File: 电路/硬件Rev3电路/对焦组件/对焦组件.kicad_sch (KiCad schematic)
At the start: 1 part, among them U1 CH32V003FxPx

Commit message: 对焦驱动几乎完成
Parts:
- removed U1: CH32V003FxPx, Package_SO:TSSOP-20_4.4x6.5mm_P0.65mm, symbol MCU_WCH_RiscV:CH32V003FxPx
- added C1, C11, C6, C7: 100nf, Capacitor_SMD:C_0603_1608Metric, symbol Device:C
- added C10, C9: 10uf, Capacitor_SMD:C_0805_2012Metric, symbol Device:C
- added C12, C13, C14, C15, C16, C17, C18: 22uf, Capacitor_SMD:C_0603_1608Metric, symbol Device:C
- added C2: 22uf, Capacitor_Tantalum_SMD:CP_EIA-3216-18_Kemet-A, symbol Device:C_Polarized
- added C3: 1uf, Capacitor_SMD:C_0603_1608Metric, symbol Device:C
- added C4, C5: 20pf, Capacitor_SMD:C_0603_1608Metric, symbol Device:C
- added C8: 47uf, Capacitor_SMD:C_0805_2012Metric, symbol Device:C
- added CN1: HX SH-1.0-8PWT, EasyEDA:CONN-SMD_8P-P1.00_HX-SH1.0-8PWT, symbol EasyEDA:HXSH-1.0-8PWT
- added CN2: HX SH-1.0-4PWT, EasyEDA:CONN-SMD_4P-HX-SH-1.0-4PWT, symbol EasyEDA:HXSH-1.0-4PWT
- added FB1: FerriteBead, Inductor_SMD:L_0603_1608Metric, symbol Device:FerriteBead
- added H1, H2, H3, H4: MountingHole, MountingHole:MountingHole_2.2mm_M2, symbol Mechanical:MountingHole
- added J1: Conn_01x04_Pin, Connector_PinHeader_1.27mm:PinHeader_1x04_P1.27mm_Vertical, symbol Connector:Conn_01x04_Pin
- added L1: 2.2uH, Inductor_SMD:L_Coilcraft_1008HQ_2520Metric, symbol Device:L
- added R1, R2, R3, R4: 10k, Resistor_SMD:R_0603_1608Metric, symbol Device:R
- added R10, R11, R6, R7, R9: 10k 1%, Resistor_SMD:R_0603_1608Metric, symbol Device:R
- added R12: 1k, Resistor_SMD:R_0603_1608Metric, symbol Device:R
- added R5: 33.2k, Resistor_SMD:R_0603_1608Metric, symbol Device:R
- added R8: 2.2k 1%, Resistor_SMD:R_0603_1608Metric, symbol Device:R
- added TH1: Thermistor_NTC, Resistor_SMD:R_0603_1608Metric, symbol Device:Thermistor_NTC
- added TP2: BOOT, TestPoint:TestPoint_Pad_D1.0mm, symbol Connector:TestPoint
- added TP3: GND, TestPoint:TestPoint_Pad_D1.0mm, symbol Connector:TestPoint
- added TP4: 3.3V, TestPoint:TestPoint_Pad_D1.0mm, symbol Connector:TestPoint
- added TP5: NRST, TestPoint:TestPoint_Pad_D1.0mm, symbol Connector:TestPoint
- added TP6: VREF, TestPoint:TestPoint_Pad_D1.0mm, symbol Connector:TestPoint
- added U1: DRV8251ADDAR, EasyEDA:SOPOWERPAD-8_L4.9-W3.9-P1.27-LS6.0-TL-EP, symbol EasyEDA:DRV8251ADDAR
- added U2: STM32F030F4Px, Package_SO:TSSOP-20_4.4x6.5mm_P0.65mm, symbol MCU_ST_STM32F0:STM32F030F4Px
- added U3: TPS563201, Package_TO_SOT_SMD:SOT-23-6, symbol Regulator_Switching:TPS563201
- added Y1: 8Mhz, Crystal:Crystal_SMD_5032-2Pin_5.0x3.2mm, symbol Device:Crystal
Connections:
- new net: R4.1, R5.2, U3.4 (VFB)
- new net: TP5.1, U2.4 (NRST)
- new net: R12.2, R2.1, U1.1 (IPROPI)
- new net: C6.1, FB1.2, TP6.1, U2.5 (VDDA)
- new net: R1.2, TP2.1, U2.1 (BOOT0)
- new net: R3.1, U3.5 (EN)
- new net: C4.1, U2.2 (PF0), Y1.2
- new net: C5.1, U2.3 (PF1), Y1.1
- new net: C11.1, L1.1, U3.2 (SW)
- new net: C11.2, U3.6 (VBST)
- new net +3V3: C1.1, C12.1, C13.1, C14.1, C2.1, C3.1, FB1.1, J1.1 (Pin_1), L1.2, R10.2, R11.2, R5.1, R8.2, TP4.1, U1.4 (VREF), U2.16 (VDD)
- new net +6V: C10.1, C7.1, C8.1, C9.1, CN1.6, CN1.7, CN1.8, R3.2, R6.2, U1.5 (VM), U3.3 (VIN)
- new net ADC_3V3: C16.1, R8.1, R9.2, U2.7 (PA1)
- new net ADC_6V: C15.1, R6.1, R7.2, U2.11 (PA5)
- new net ADC_MT: R12.1, U2.12 (PA6)
- new net ADC_NTC1: C18.1, CN2.3, R10.1, U2.6 (PA0)
- new net ADC_NTC2: C17.1, R11.1, TH1.1, U2.10 (PA4)
- new net GND: C1.2, C10.2, C12.2, C13.2, C14.2, C15.2, C16.2, C17.2, C18.2, C2.2, C3.2, C4.2, C5.2, C6.2, C7.2, C8.2, C9.2, CN1.1, CN1.2, CN1.3, CN2.4, J1.4 (Pin_4), R1.1, R2.2, R4.2, R7.1, R9.1, TH1.2, TP3.1, U1.7 (GND), U1.9 (PAD), U2.15 (VSS), U3.1 (GND)
- new net MOT_A: CN2.1, U1.6 (OUT1)
- new net MOT_B: CN2.2, U1.8 (OUT2)
- new net MotorPWM_A: U1.3 (IN1), U2.18 (PA10)
- new net MotorPWM_B: U1.2 (IN2), U2.17 (PA9)
- new net SWCLK: J1.3 (Pin_3), U2.20 (PA14)
- new net SWDIO: J1.2 (Pin_2), U2.19 (PA13)
- new net USART1 _RX: CN1.4, U2.9 (PA3)
- new net USART1 _TX: CN1.5, U2.8 (PA2)
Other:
- note added: "ADC_IN0"
- note added: "ADC_IN1"
- note added: "ADC_IN4"
- note added: "ADC_IN5"
- note added: "ADC_IN6"
- note added: "TIM1_CH2"
- note added: "TIM1_CH3"

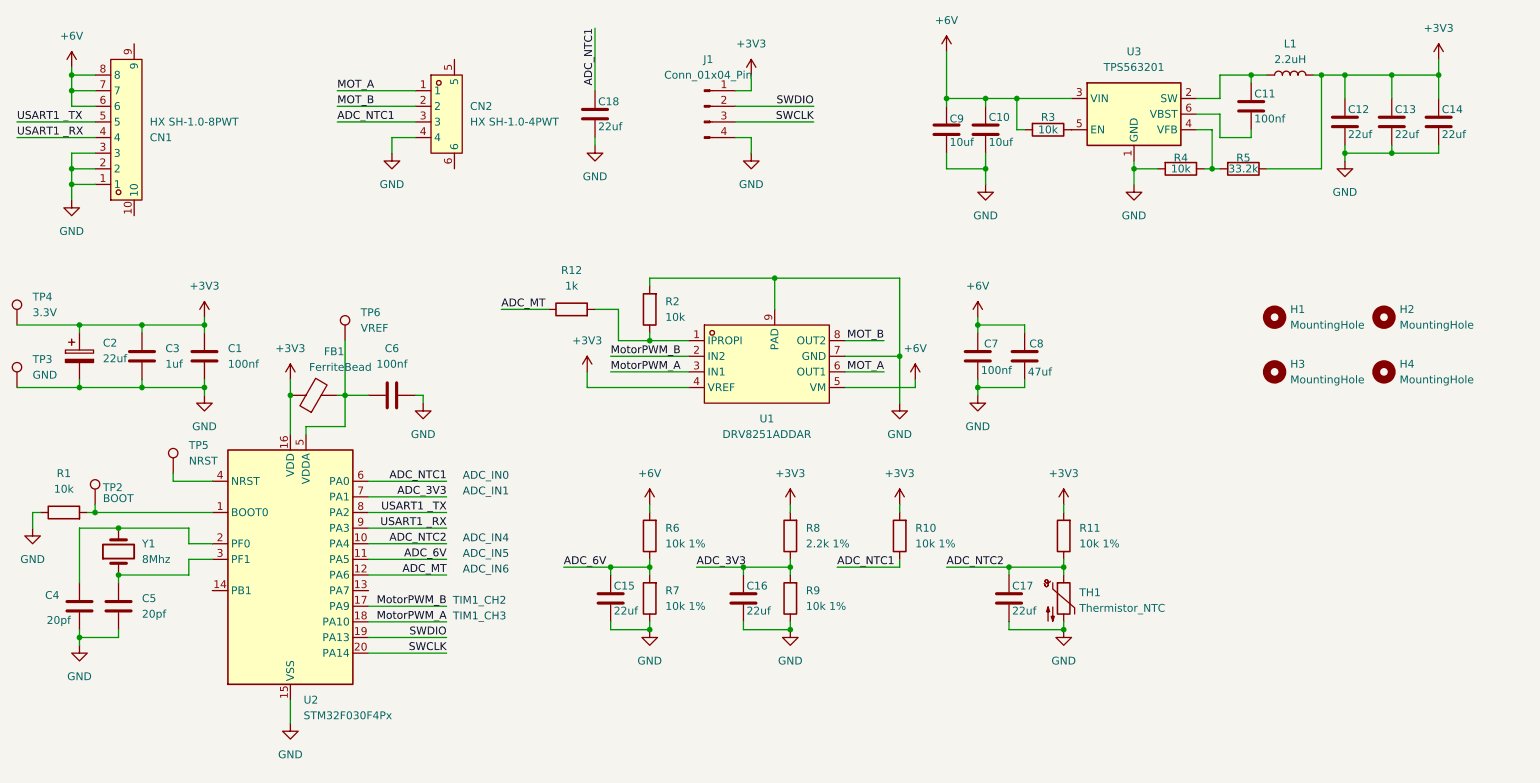
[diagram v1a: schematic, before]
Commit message: 对焦组件R1投产，对焦机构开始测试
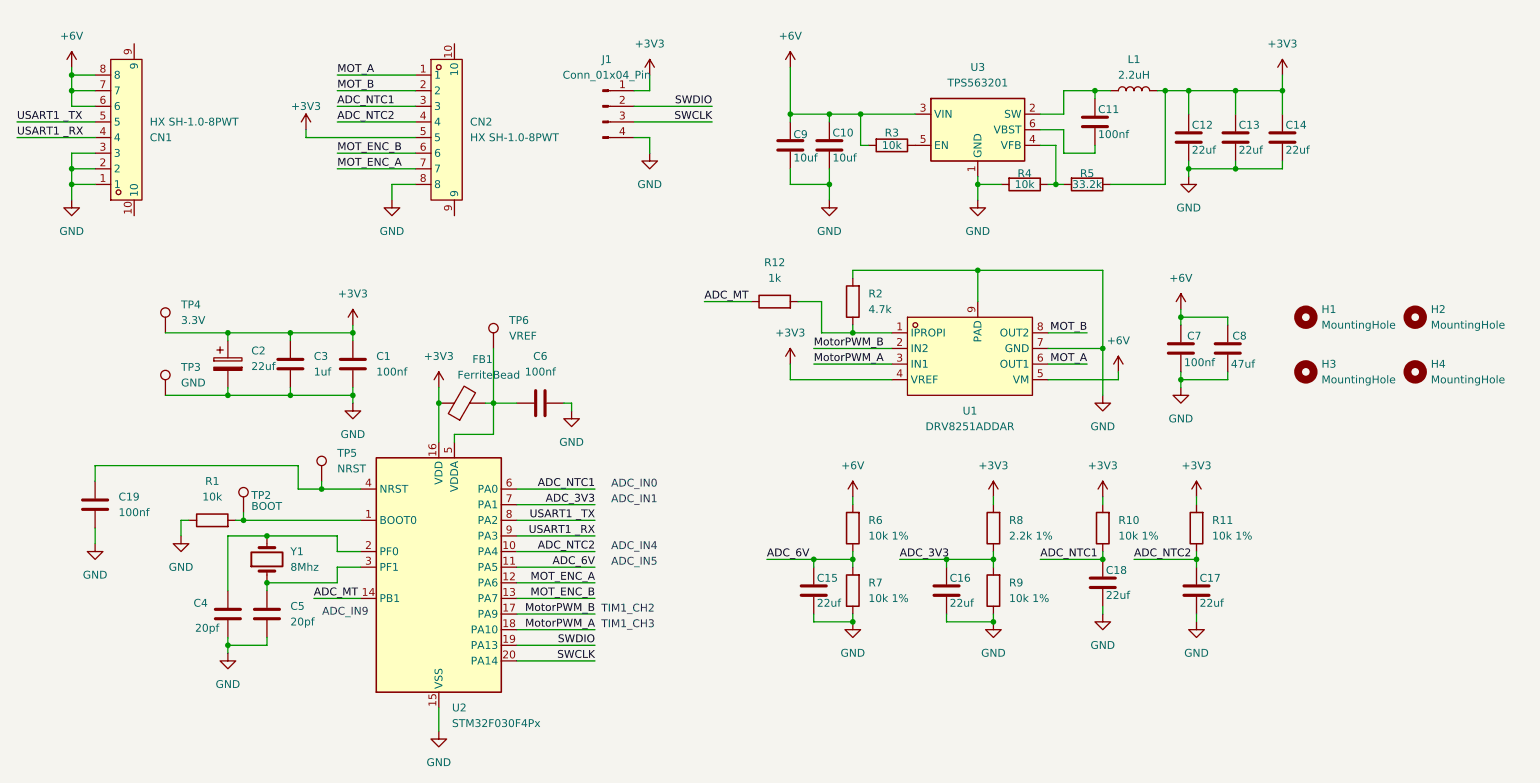
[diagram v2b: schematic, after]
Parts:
- removed CN2: HX SH-1.0-4PWT, EasyEDA:CONN-SMD_4P-HX-SH-1.0-4PWT, symbol EasyEDA:HXSH-1.0-4PWT
- removed TH1: Thermistor_NTC, Resistor_SMD:R_0603_1608Metric, symbol Device:Thermistor_NTC
- added C19: 100nf, Capacitor_SMD:C_0603_1608Metric, symbol Device:C
- added CN2: HX SH-1.0-8PWT, EasyEDA:CONN-SMD_8P-P1.00_HX-SH1.0-8PWT, symbol EasyEDA:HXSH-1.0-8PWT
- R2: value 10k -> 4.7k
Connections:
- net +3V3: now also CN2.5
- net ADC_MT: now also U2.14 (PB1); no longer U2.12 (PA6)
- net ADC_NTC1: now also CN2.3
- net ADC_NTC2: now also CN2.4
- net GND: now also C19.2, CN2.8
- net MOT_A: now also CN2.1
- net MOT_B: now also CN2.2
- net at TP5.1, U2.4 (NRST): now also C19.1
- net MOT_ENC_B: now reaches U2.13 (PA7)
- net MOT_ENC_B: now also CN2.6
- new net MOT_ENC_A: CN2.7, U2.12 (PA6)
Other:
- note added: "ADC_IN9"
- note removed: "ADC_IN6"
- title: (none) -> Focus Unit Drive
- moved on the sheet: C1, C10, C11, C12, C13, C14, C15, C16, C17, C18, C2, C3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
